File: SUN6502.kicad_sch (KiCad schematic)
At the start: 10 parts, among them SW1 RESET, U1 W65C02SxP, U2 KM62256CLP, U3 28C256, U5 74LS139, U6 74LS138, Y1 1Mhz

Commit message: updates
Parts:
- added C2, C3, C4, C5, C6, C8: 100nf, symbol Device:C
- added C7: 100uF, symbol Device:C_Polarized
- added J1: Barrel_Jack_MountingPin, Connector_BarrelJack:BarrelJack_Horizontal, symbol Connector:Barrel_Jack_MountingPin
- added SW2: SW_SPST, symbol Switch:SW_SPST
- added U4, U7: W65C22NxP, Package_DIP:DIP-40_W15.24mm, symbol PCM_65xx-library:W65C22NxP
- added U8: W65C51NxP, Package_DIP:DIP-28_W15.24mm, symbol PCM_65xx-library:W65C51NxP
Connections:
- net +5V: now also C2.2, C3.2, C4.2, C5.2, C6.2, C7.1, C8.2, SW2.2 (B), U4.20 (VCC), U7.20 (VCC), U8.15 (VCC)
- net Address Bus: now also U1.39 (ϕ2), Y1.8 (OUT), U8.27 (ϕ2)
- net GND: now also C2.1, C3.1, C4.1, C5.1, C6.1, C7.2, C8.1, J1.2, J1.MP (MountPin), U8.1 (VSS)
- net d0: now also U4.33 (D0), U7.33 (D0), U8.18 (D0)
- net d1: now also U4.32 (D1), U7.32 (D1), U8.19 (D1)
- net d2: now also U4.31 (D2), U7.31 (D2), U8.20 (D2)
- net d3: now also U4.30 (D3), U7.30 (D3), U8.21 (D3)
- net d4: now also U4.29 (D4), U7.29 (D4), U8.22 (D4)
- net d5: now also U4.28 (D5), U7.28 (D5), U8.23 (D5)
- net d6: now also U4.27 (D6), U7.27 (D6), U8.24 (D6)
- net d7: now also U4.26 (D7), U7.26 (D7), U8.25 (D7)
- new net: J1.1, SW2.1 (A)
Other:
- company: (none) -> Wróbel Sebastian (Aktr0s)
- title: (none) -> Sun6502 Computer
- moved on the sheet: U5A, U6

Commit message: updates, removed backup files
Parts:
- removed U6: 74LS138, symbol 74xx:74LS138
- added BZ1: Buzzer, Buzzer_Beeper:Buzzer_12x9.5RM7.6, symbol Device:Buzzer
- added C10, C11, C12, C13, C9: 100nf, symbol Device:C
- added C14, C15, C16, C17: 1uF, symbol Device:C
- added D1: SB140, symbol Diode:SB140
- added D2, D3: SB140, Diode_THT:D_DO-41_SOD81_P10.16mm_Horizontal, symbol Diode:SB140
- added DS1: WC1602A, Display:WC1602A, symbol Display_Character:WC1602A
- added J2, J3: 6-5530843-5, 6-5530843-5:TE_6-5530843-5, symbol 6-5530843-5:6-5530843-5
- added J4: DE9_Socket, symbol Connector:DE9_Socket
- added R3: 1K, symbol Device:R
- added RV1: R_Potentiometer, symbol Device:R_Potentiometer
- added U10: MAX232, symbol Interface_UART:MAX232
- added unit 3 of U5
- added U6: 74LS21, symbol 74xx:74LS21
- added U9: 74LS138, symbol 74xx:74LS138
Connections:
- net +5V: now also C2.1, U4.24 (CS1), U7.24 (CS1), U8.2 (CS1), C10.2, C11.2, C12.2, C13.2, C9.2, DS1.15 (LED(+)), DS1.2 (VDD), J2.1, J2.2, U10.16 (VCC), U5.16 (VCC), U6.1, U6.14 (VCC), U9.16 (VCC); no longer C2.2
- net Address Bus: no longer U1.39 (ϕ2), U8.27 (ϕ2), Y1.8 (OUT)
- net GND: now also C2.2, U3.1 (A14), U4.1 (VSS), BZ1.2 (-), C10.1, C11.1, C12.1, C13.1, C16.2, C17.2, C9.1, DS1.1 (VSS), DS1.16 (LED(-)), J2.61, J2.62, J4.5, RV1.1, U10.15 (GND), U5.8 (GND), U6.7 (GND), U9.4 (E1), U9.5 (E2), U9.8 (GND); no longer C2.1
- net a0: now also U4.38 (RS0), U8.13 (RS0)
- net a1: now also U4.37 (RS1), U8.14 (RS1)
- net a10: now also U5.3 (A1)
- net a11: now also U5.2 (A0)
- net a12: now also U9.1 (A0)
- net a13: now also U9.2 (A1)
- net a14: now also U9.3 (A2); no longer U3.1 (A14)
- net a15: now also U2.20 (~{CS}), U2.22 (~{OE}), U9.6 (E3)
- net a2: now also U4.36 (RS2)
- net a3: now also U4.35 (RS3)
- net at C1.1, R1.2, SW1.2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: now also U4.34 (~{RES}), U7.34 (~{RES}), U8.4 (~{RES})
- net at U5.1 (E): now also U9.15 (O0)
- net at U5.4 (O0): now also U4.23 (~{CS2})
- net at U5.5 (O1): now also U7.23 (~{CS2})
- net at U5.6 (O2): now also U8.3 (~{CS2})
- net at R2.2, U1.2 (RDY): now also U1.34 (R/~{W}), U4.22 (R/~{W}), U7.22 (R/~{W}), U8.28 (R/~{W})
- net at U1.4 (~{IRQ}): now also D1.2 (A), D2.2 (A), D3.2 (A)
- net at U3.20 (~{CS}): now also U6.8
- net at U8.26 (~{IRQ}): now also D3.1 (K)
- net at U7.21 (~{IRQ}): now also D2.1 (K)
- net at U7.25 (ϕ2): now also U1.39 (ϕ2), U4.25 (ϕ2), U8.27 (ϕ2), Y1.8 (OUT)
- net at U4.10 (PB0): now also DS1.7 (D0)
- net at U4.11 (PB1): now also DS1.8 (D1)
- net at U4.12 (PB2): now also DS1.9 (D2)
- net at U4.13 (PB3): now also DS1.10 (D3)
- net at U4.14 (PB4): now also DS1.11 (D4)
- net at U4.15 (PB5): now also DS1.12 (D5)
- net at U4.16 (PB6): now also DS1.13 (D6)
- net at U4.17 (PB7): now also DS1.14 (D7)
- net at U4.2 (PA0): now also R3.1
- net at U4.21 (~{IRQ}): now also D1.1 (K)
- net at U4.7 (PA5): now also DS1.4 (RS)
- net at U4.8 (PA6): now also DS1.5 (R/W)
- net at U4.9 (PA7): now also DS1.6 (E)
- new net: J4.2, U10.14 (T1OUT)
- new net: J4.3, U10.13 (R1IN)
- new net: C16.1, U10.2 (VS+)
- new net: C15.1, U10.4 (C2+)
- new net: C15.2, U10.5 (C2-)
- new net: U6.2, U9.14 (O1)
- new net: U6.4, U9.13 (O2)
- new net: U6.5, U9.12 (O3)
- new net: C17.1, U10.6 (VS-)
- new net: C14.1, U10.1 (C1+)
- new net: C14.2, U10.3 (C1-)
- new net: BZ1.1 (+), R3.2
- new net: DS1.3 (VO), RV1.2
- new net: U6.10, U9.10 (O5)
- new net: U6.12, U9.9 (O6)
- new net: U6.13, U9.7 (O7)
- new net: U6.9, U9.11 (O4)
- no-connect marks 7 -> 27
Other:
- note added: "(CS) to Expansion Bus (Active low)"
- note added: "Unused 1K"
- moved on the sheet: C2, C3, C4, C5, C6, C7, C8, J1, R2, SW2, U1, U2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

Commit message: updates
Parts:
- removed C12: 100nf, symbol Device:C
- added C18: 20pf, symbol Device:C
- added C20: 100nf, symbol Device:C
- added D6: SB140, Diode_THT:D_DO-41_SOD81_P10.16mm_Horizontal, symbol Diode:SB140
- added R4: 1M, symbol Device:R
- added U11: 74LS00, symbol 74xx:74LS00
- added Y2: 1.8432Mhz, symbol Device:Crystal
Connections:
- net +5V: now also J3.61, J3.62, C20.2, U11.14 (VCC)
- net GND: now also J3.1, J3.2, U7.1 (VSS), C18.1, C20.1, U11.7 (GND)
- net a0: now also J3.3, U7.38 (RS0)
- net a1: now also J3.5, U7.37 (RS1)
- net a10: now also J3.23
- net a11: now also J3.25
- net a12: now also J3.27
- net a13: now also J3.29
- net a2: now also J3.7, U7.36 (RS2)
- net a3: now also J3.9, U7.35 (RS3)
- net a4: now also J3.11
- net a5: now also J3.13
- net a6: now also J3.15
- net a7: now also J3.17
- net a8: now also J3.19
- net a9: now also J3.21
- net d0: now also J3.59
- net d1: now also J3.57
- net d2: now also J3.55
- net d3: now also J3.53
- net d4: now also J3.51
- net d5: now also J3.49
- net d6: now also J3.47
- net d7: now also J3.45
- net at C1.1, R1.2, SW1.2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: now also J3.4, J3.60
- net at U4.25 (ϕ2), U7.25 (ϕ2), U8.27 (ϕ2)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: now also J3.58, J3.6, U1.37 (ϕ0), U11.5; no longer U1.39 (ϕ2)
- net at J3.10: now also J3.54, U1.34 (R/~{W}), U4.22 (R/~{W}), U7.22 (R/~{W}), U8.28 (R/~{W}), U11.1, U11.2
- net at J3.12: now also J3.52, U6.6
- net at J3.14: now also J3.50, R2.2, U1.2 (RDY)
- net at J3.56: now also J3.8, D6.1 (K)
- net at U2.27 (~{WE}): now also U11.6
- net at D1.2 (A), D2.2 (A), D3.2 (A)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: now also D6.2 (A)
- net at U10.11 (T1IN): now also U8.10 (TxD)
- net at U10.12 (R1OUT): now also U8.12 (RxD)
- net at U8.6 (XTAL1): now also C18.2, R4.1, Y2.2
- net at U8.7 (XTAL2): now also R4.2, Y2.1
- net at J2.11: now also U7.6 (PA4)
- net at J2.13: now also U7.7 (PA5)
- net at J2.15: now also U7.8 (PA6)
- net at J2.17: now also U7.9 (PA7)
- net at J2.21: now also U7.40 (CA1)
- net at J2.23: now also U7.39 (CA2)
- net at J2.3: now also U7.2 (PA0)
- net at J2.40: now also U7.19 (CB2)
- net at J2.42: now also U7.18 (CB1)
- net at J2.46: now also U7.17 (PB7)
- net at J2.48: now also U7.16 (PB6)
- net at J2.5: now also U7.3 (PA1)
- net at J2.50: now also U7.15 (PB5)
- net at J2.52: now also U7.14 (PB4)
- net at J2.54: now also U7.13 (PB3)
- net at J2.56: now also U7.12 (PB2)
- net at J2.58: now also U7.11 (PB1)
- net at J2.60: now also U7.10 (PB0)
- net at J2.7: now also U7.4 (PA2)
- net at J2.9: now also U7.5 (PA3)
- new net: U11.3, U11.4
- no-connect marks 27 -> 100
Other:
- note added: "Address Bus"
- note added: "Data Bus"
- note added: "Expansion Bus Port"
- note added: "VIA Expansion Port"
- note removed: "(CS) to Expansion Bus (Active low)"
- moved on the sheet: C16, C17, DS1, J2, J3, J4, R2, RV1

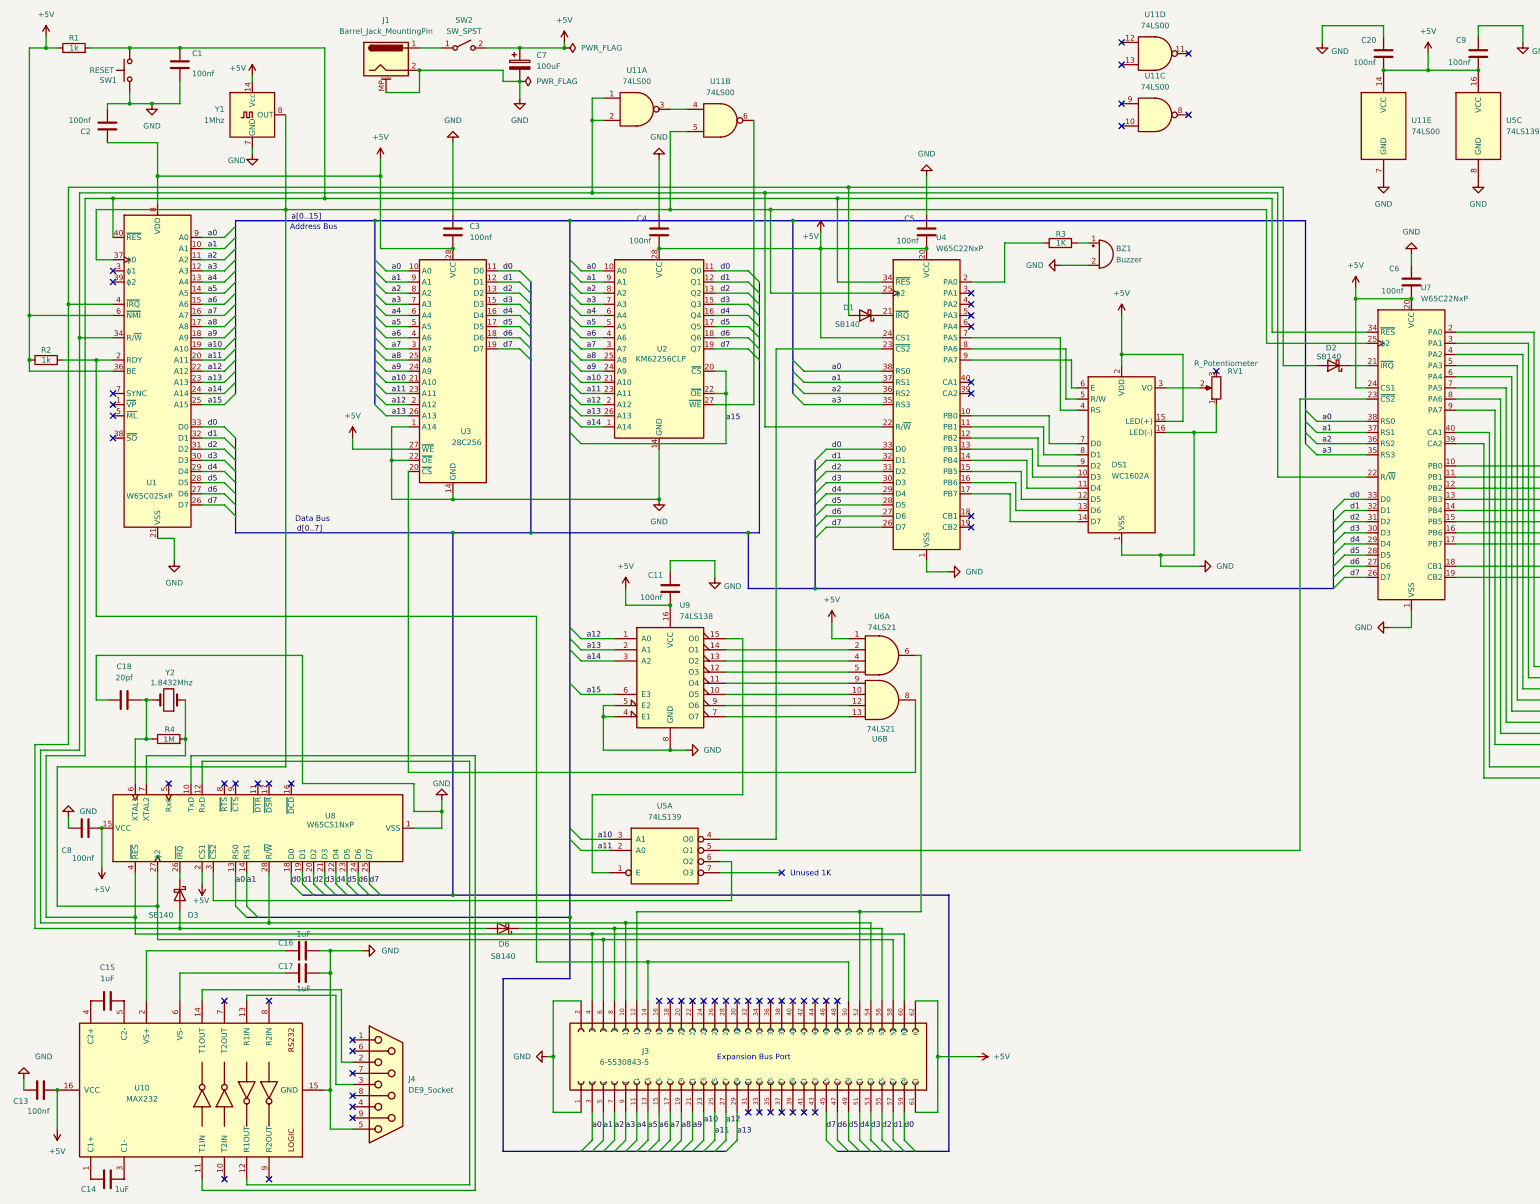
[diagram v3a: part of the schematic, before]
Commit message: updates, schematic more or less ready for pcb mapping
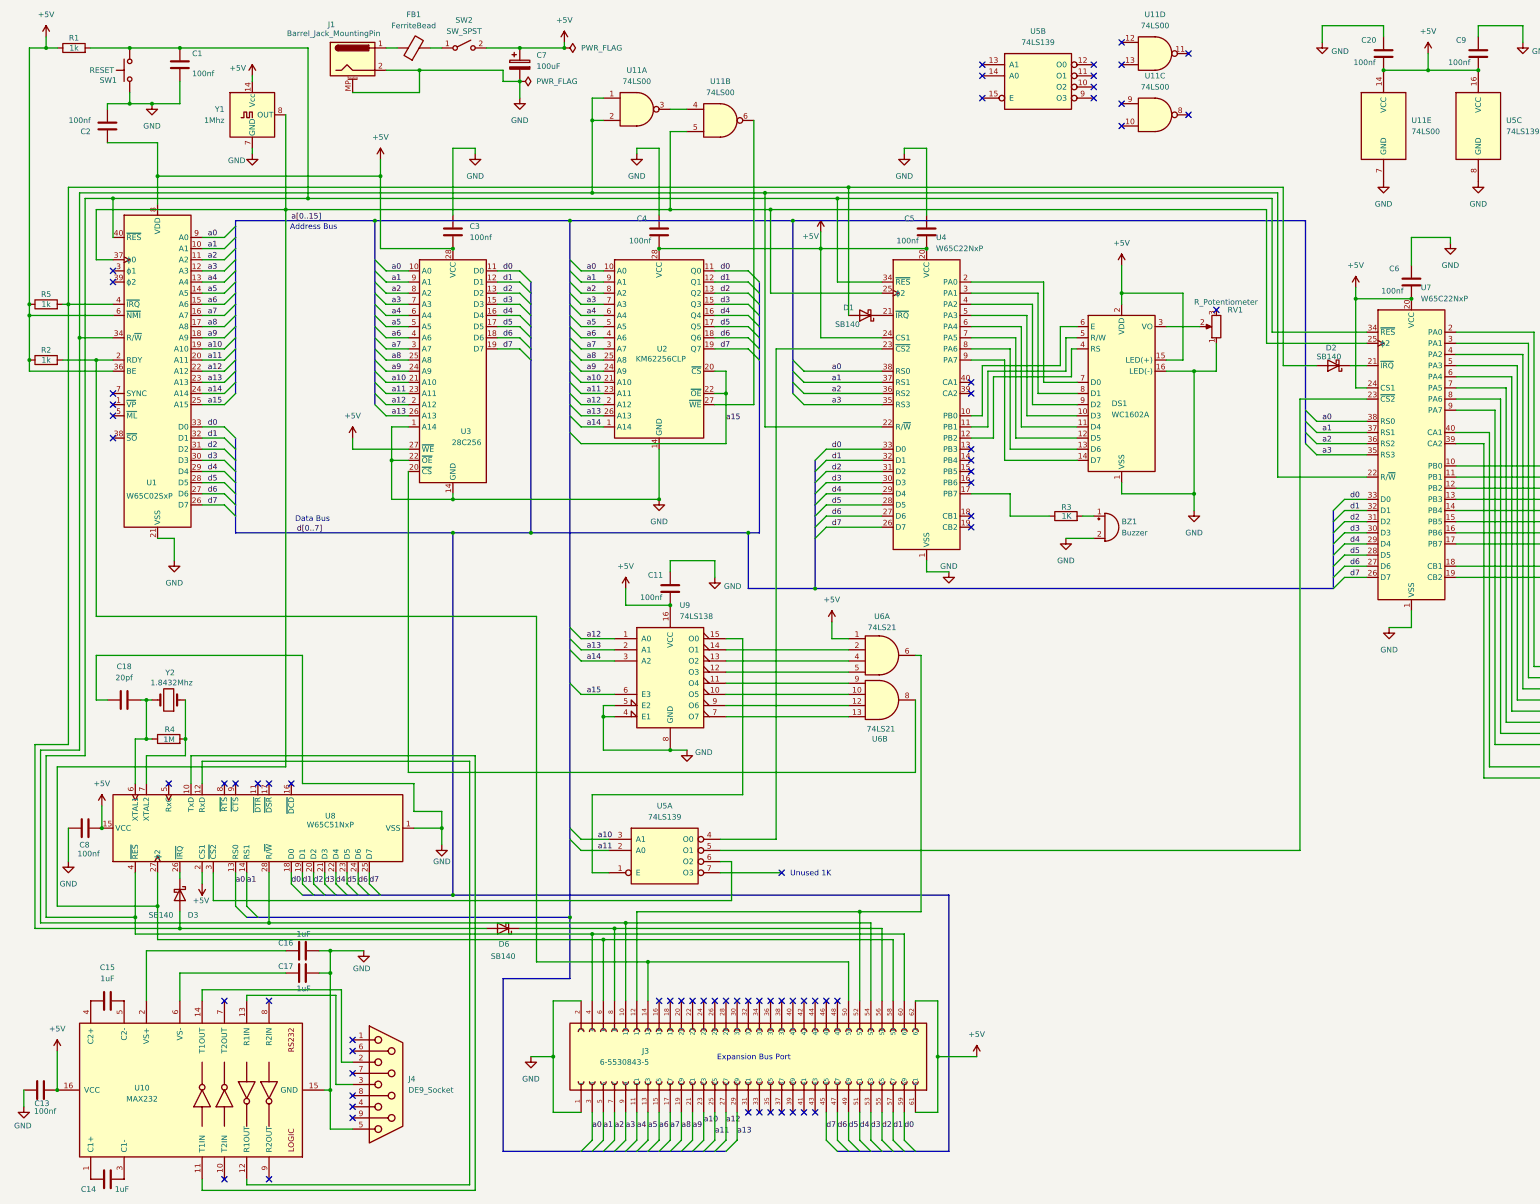
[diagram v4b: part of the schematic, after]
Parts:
- added FB1: FerriteBead, Ferrite_THT:LairdTech_28C0236-0JW-10, symbol Device:FerriteBead
- added R5: 1k, symbol Device:R
- BZ1: footprint Buzzer_Beeper:Buzzer_12x9.5RM7.6 -> Buzzer_Beeper:Buzzer_TDK_PS1240P02BT_D12.2mm_H6.5mm
- J2, J3: footprint 6-5530843-5:TE_6-5530843-5 -> footprints:TE_6-5530843-5
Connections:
- net +5V: now also R5.1
- net at D1.2 (A), D2.2 (A), D3.2 (A)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: now also R5.2
- net at R3.1: now also U4.17 (PB7); no longer U4.2 (PA0)
- net at J1.1: now also FB1.1; no longer SW2.1 (A)
- net at U4.10 (PB0): now also DS1.6 (E); no longer DS1.7 (D0)
- net at U4.11 (PB1): now also DS1.5 (R/W); no longer DS1.8 (D1)
- net at U4.12 (PB2): now also DS1.4 (RS); no longer DS1.9 (D2)
- net at U4.13 (PB3): no longer DS1.10 (D3)
- net at U4.14 (PB4): no longer DS1.11 (D4)
- net at U4.15 (PB5): no longer DS1.12 (D5)
- net at U4.16 (PB6): no longer DS1.13 (D6)
- net at DS1.14 (D7): now also U4.9 (PA7); no longer U4.17 (PB7)
- net at U4.3 (PA1): now also DS1.8 (D1)
- net at U4.4 (PA2): now also DS1.9 (D2)
- net at U4.5 (PA3): now also DS1.10 (D3)
- net at U4.6 (PA4): now also DS1.11 (D4)
- net at U4.7 (PA5): now also DS1.12 (D5); no longer DS1.4 (RS)
- net at U4.8 (PA6): now also DS1.13 (D6); no longer DS1.5 (R/W)
- new net: FB1.2, SW2.1 (A)
- new net: DS1.7 (D0), U4.2 (PA0)
- no-connect marks 100 -> 107
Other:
- moved on the sheet: BZ1, DS1, J1, R3, RV1

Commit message: pcb layout done
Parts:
- added D4: LED, LED_THT:LED_D5.0mm, symbol Device:LED
- added R6: 250, Resistor_THT:R_Axial_DIN0207_L6.3mm_D2.5mm_P10.16mm_Horizontal, symbol Device:R
- added unit 2 of U5
- C1, C10, C11, C13, C14, C15, C16, C17, C2, C3, C4, C5, C6, C8, C9: footprint (none) -> Capacitor_THT:C_Disc_D5.0mm_W2.5mm_P5.00mm
- C18: footprint (none) -> Capacitor_THT:C_Disc_D5.0mm_W2.5mm_P2.50mm
- C20: footprint (none) -> Capacitor_THT:C_Disc_D4.7mm_W2.5mm_P5.00mm
- C7: footprint (none) -> Capacitor_THT:CP_Radial_D6.3mm_P2.50mm
- D1: footprint (none) -> Diode_THT:D_DO-41_SOD81_P10.16mm_Horizontal
- J1: symbol Connector:Barrel_Jack_MountingPin -> Connector:Barrel_Jack
- J4: footprint (none) -> Connector_Dsub:DSUB-9_Socket_Horizontal_P2.77x2.84mm_EdgePinOffset7.70mm_Housed_MountingHolesOffset9.12mm
- R1, R2, R5: footprint (none) -> Resistor_THT:R_Axial_DIN0207_L6.3mm_D2.5mm_P15.24mm_Horizontal
- R3: value 1K -> 1k; footprint (none) -> Resistor_THT:R_Axial_DIN0207_L6.3mm_D2.5mm_P15.24mm_Horizontal
- R4: footprint (none) -> Resistor_THT:R_Axial_DIN0309_L9.0mm_D3.2mm_P20.32mm_Horizontal
- RV1: footprint (none) -> Potentiometer_THT:Potentiometer_Alps_RK09K_Single_Vertical
- SW1: footprint (none) -> Button_Switch_THT:SW_PUSH_6mm_H5mm
- SW2: value SW_SPST -> Power Switch; footprint (none) -> footprints:2MS6T1B3M2QES
- U1, U4, U7: footprint Package_DIP:DIP-40_W15.24mm -> Package_DIP:DIP-40_W15.24mm_Socket_LongPads
- U10, U5, U9: footprint (none) -> Package_DIP:DIP-16_W7.62mm_Socket_LongPads
- U11, U6: footprint (none) -> Package_DIP:DIP-14_W7.62mm_Socket_LongPads
- U2, U3: footprint (none) -> Package_DIP:DIP-28_W15.24mm_Socket_LongPads
- U8: footprint Package_DIP:DIP-28_W15.24mm -> Package_DIP:DIP-28_W15.24mm_Socket_LongPads
- Y2: footprint (none) -> Crystal:Crystal_HC18-U_Vertical
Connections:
- net +5V: now also R6.1
- net GND: now also D4.1 (K); no longer J1.MP (MountPin)
- new net: D4.2 (A), R6.2

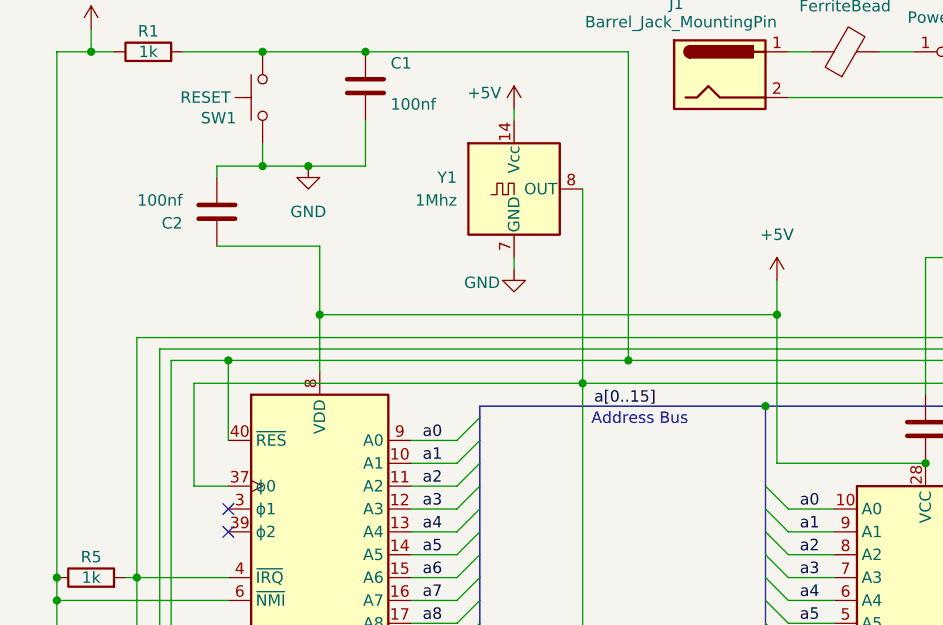
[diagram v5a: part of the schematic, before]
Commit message: updates, changed ROM socket into ZIF
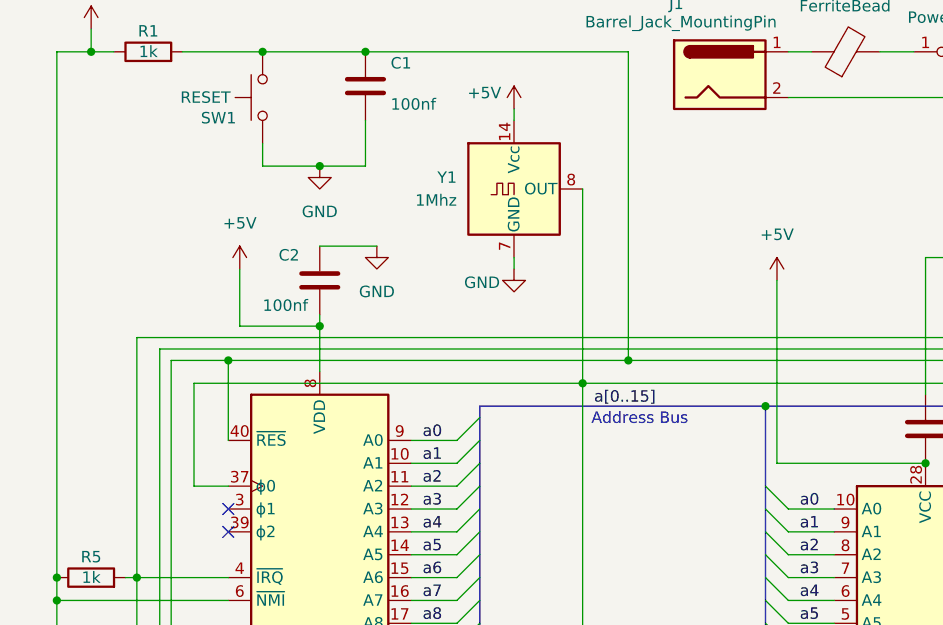
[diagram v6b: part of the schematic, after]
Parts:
- U3: footprint Package_DIP:DIP-28_W15.24mm_Socket_LongPads -> Socket:DIP_Socket-28_W11.9_W12.7_W15.24_W17.78_W18.5_3M_228-1277-00-0602J
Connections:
- net +5V: now also C2.2; no longer C2.1
- net GND: now also C2.1; no longer C2.2
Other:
- moved on the sheet: C2
